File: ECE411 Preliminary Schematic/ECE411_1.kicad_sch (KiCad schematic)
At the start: 12 parts, among them J2 Raspberry_Pi_4, M1 Motor_Servo, U1 XVF3800 (XM-014888-PC)

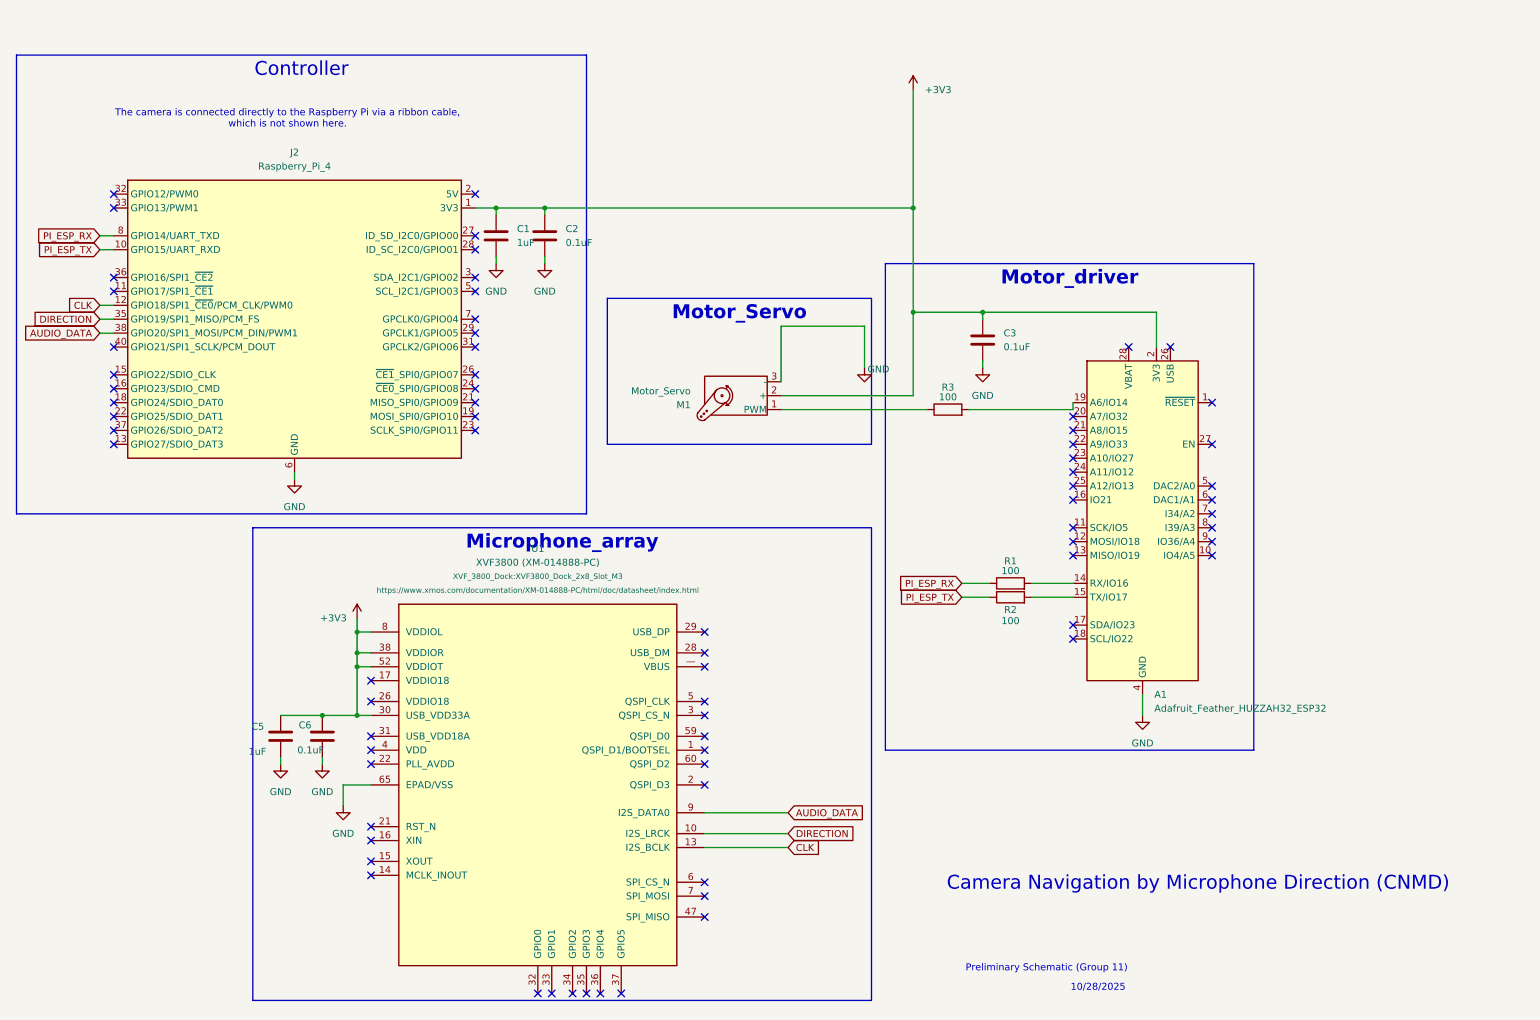
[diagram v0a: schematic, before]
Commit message: update the PCB design to 3.0
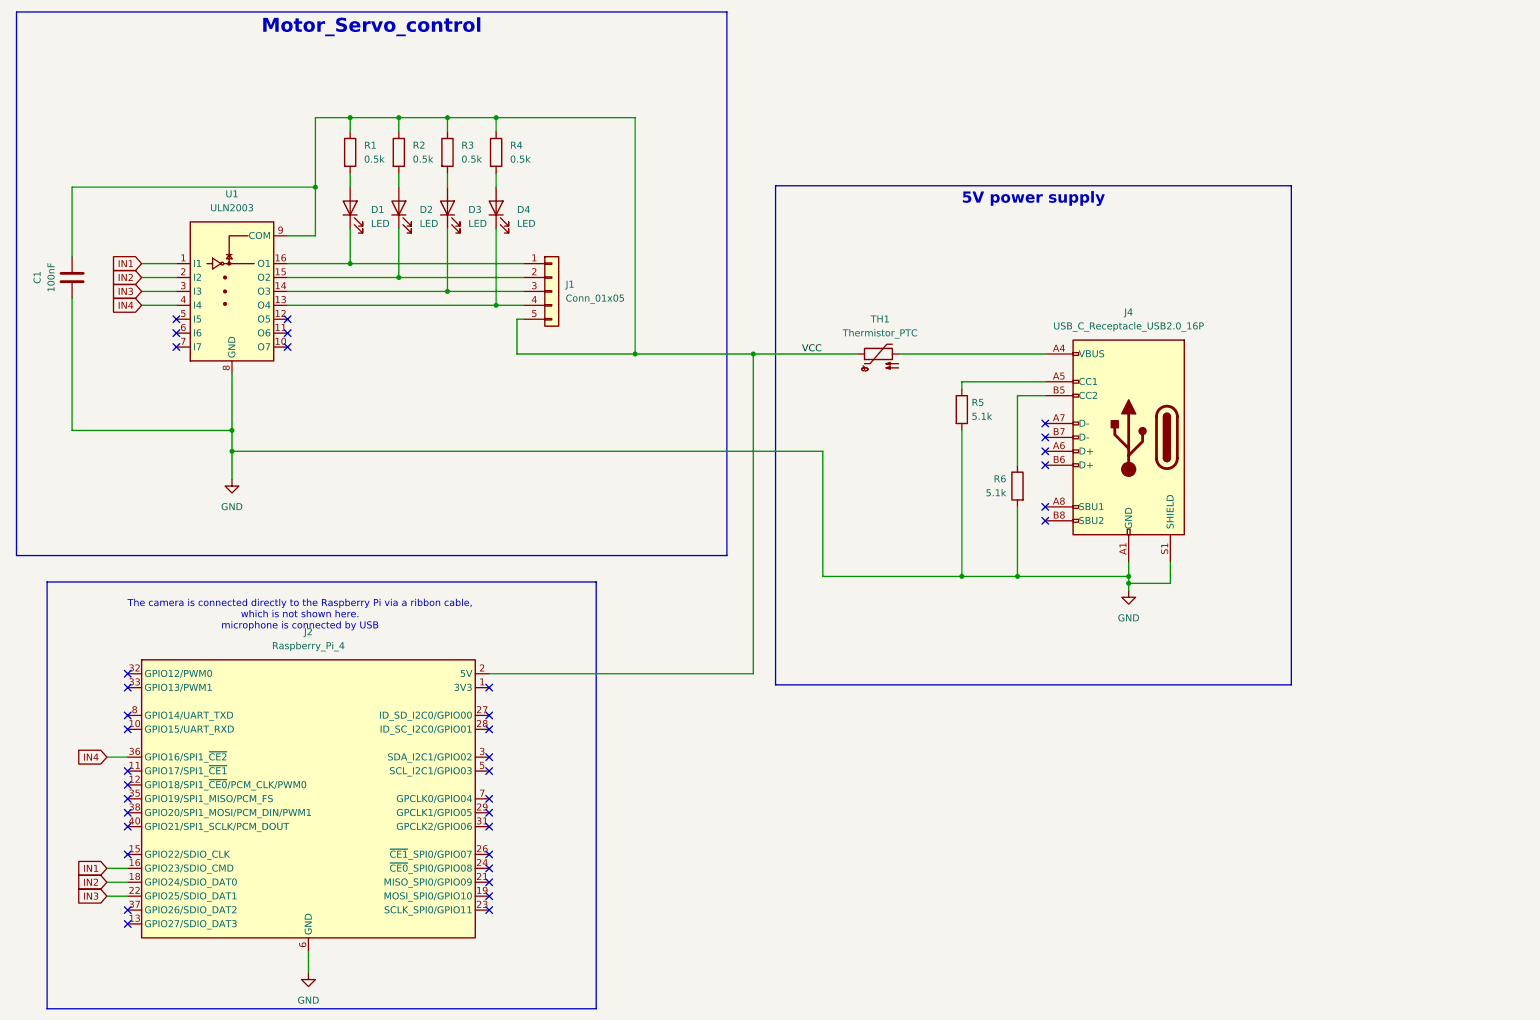
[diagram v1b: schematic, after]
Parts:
- removed A1: Adafruit_Feather_HUZZAH32_ESP32, Module:Adafruit_Feather, symbol MCU_Module:Adafruit_Feather_HUZZAH32_ESP32
- removed C2, C3, C6: 0.1uF, Capacitor_SMD:C_0603_1608Metric, symbol Device:C
- removed C5: 1uF, Capacitor_SMD:C_0603_1608Metric, symbol Device:C
- removed M1: Motor_Servo, Connector_PinHeader_2.54mm:PinHeader_1x03_P2.54mm_Vertical, symbol Motor:Motor_Servo
- removed U1: XVF3800 (XM-014888-PC), XVF_3800_Dock:XVF3800_Dock_2x8_Slot_M3, symbol XMOS_Custom:XVF3800
- added D1, D2, D3, D4: LED, LED_THT:LED_D3.0mm, symbol Device:LED
- added J1: Conn_01x05, Connector_JST:JST_XH_B5B-XH-A_1x05_P2.50mm_Vertical, symbol Connector_Generic:Conn_01x05
- added J4: USB_C_Receptacle_USB2.0_16P, Connector_USB:USB_C_Receptacle_GCT_USB4105-xx-A_16P_TopMnt_Horizontal, symbol Connector:USB_C_Receptacle_USB2.0_16P
- added R4: 0.5k, Resistor_SMD:R_0805_2012Metric_Pad1.20x1.40mm_HandSolder, symbol Device:R
- added R5, R6: 5.1k, Resistor_SMD:R_0805_2012Metric_Pad1.20x1.40mm_HandSolder, symbol Device:R
- added TH1: Thermistor_PTC, Fuse:Fuse_Bourns_MF-RHT300, symbol Device:Thermistor_PTC
- added U1: ULN2003, Package_DIP:DIP-16_W7.62mm_LongPads, symbol Transistor_Array:ULN2003
- C1: value 1uF -> 100nF; footprint Capacitor_SMD:C_0603_1608Metric -> Capacitor_SMD:C_0805_2012Metric_Pad1.18x1.45mm_HandSolder
- J2: footprint Module:Raspberry_Pi_Zero_Socketed_THT_FaceDown_MountingHoles -> XVF_3800_Dock:rap5
- R1, R2, R3: value 100 -> 0.5k; footprint Resistor_SMD:R_0603_1608Metric -> Resistor_SMD:R_0805_2012Metric_Pad1.20x1.40mm_HandSolder
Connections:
- net GND: now also C1.1, J4.A1 (GND), J4.A12 (GND), J4.B1 (GND), J4.B12 (GND), J4.S1 (SHIELD), R5.2, R6.2, U1.8 (GND); no longer C1.2
- net at R1.2: now also D1.2 (A)
- net at R2.2: now also D2.2 (A)
- net at R3.2: now also D3.2 (A)
- net VCC: now reaches R3.1
- net VCC: now also C1.2, J2.2 (5V), J2.4 (5V), R1.1, R2.1, J1.5 (Pin_5), R4.1, TH1.1, U1.9 (COM)
- net IN1: now reaches J2.16 (GPIO23/SDIO_CMD)
- net IN1: now also U1.1 (I1)
- net IN2: now reaches J2.18 (GPIO24/SDIO_DAT0)
- net IN2: now also U1.2 (I2)
- net IN3: now reaches J2.22 (GPIO25/SDIO_DAT1)
- net IN3: now also U1.3 (I3)
- net IN4: now reaches J2.36 (GPIO16/SPI1_~{CE2})
- net IN4: now also U1.4 (I4)
- net +3V3: no longer names the net of J2.1 (3V3), J2.17 (3V3)
- net +3V3: no longer C1.1
- net AUDIO_DATA: no longer names the net of J2.38 (GPIO20/SPI1_MOSI/PCM_DIN/PWM1)
- net CLK: no longer names the net of J2.12 (GPIO18/SPI1_~{CE0}/PCM_CLK/PWM0)
- net DIRECTION: no longer names the net of J2.35 (GPIO19/SPI1_MISO/PCM_FS)
- net PI_ESP_RX: no longer names the net of J2.8 (GPIO14/UART_TXD)
- net PI_ESP_RX: no longer R1.1
- net PI_ESP_TX: no longer names the net of J2.10 (GPIO15/UART_RXD)
- net PI_ESP_TX: no longer R2.1
- new net: J4.A4 (VBUS), J4.A9 (VBUS), J4.B4 (VBUS), J4.B9 (VBUS), TH1.2
- new net: J4.A5 (CC1), R5.1
- new net: J4.B5 (CC2), R6.1
- new net: D4.1 (K), J1.4 (Pin_4), U1.13 (O4)
- new net: D4.2 (A), R4.2
- new net: D2.1 (K), J1.2 (Pin_2), U1.15 (O2)
- new net: D3.1 (K), J1.3 (Pin_3), U1.14 (O3)
- new net: D1.1 (K), J1.1 (Pin_1), U1.16 (O1)
- no-connect marks 73 -> 37
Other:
- note added: "The camera is connected directly to the Raspberry Pi via a ribbon cable, which is not shown here. microphone is connected by USB"
- note removed: "10/28/2025"
- note removed: "Camera Navigation by Microphone Direction (CNMD)"
- note removed: "Preliminary Schematic (Group 11)"
- note removed: "The camera is connected directly to the Raspberry Pi via a ribbon cable, which is not shown here."
- title: (none) -> Camera Navigation by Microphone Direction
- moved on the sheet: J2
